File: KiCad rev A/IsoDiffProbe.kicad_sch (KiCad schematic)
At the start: 82 parts, among them J1 USB C 6-Pin, J2 SMA Conn, P1 Header 10X2, U1 AMC33xx, U2 OPA2376

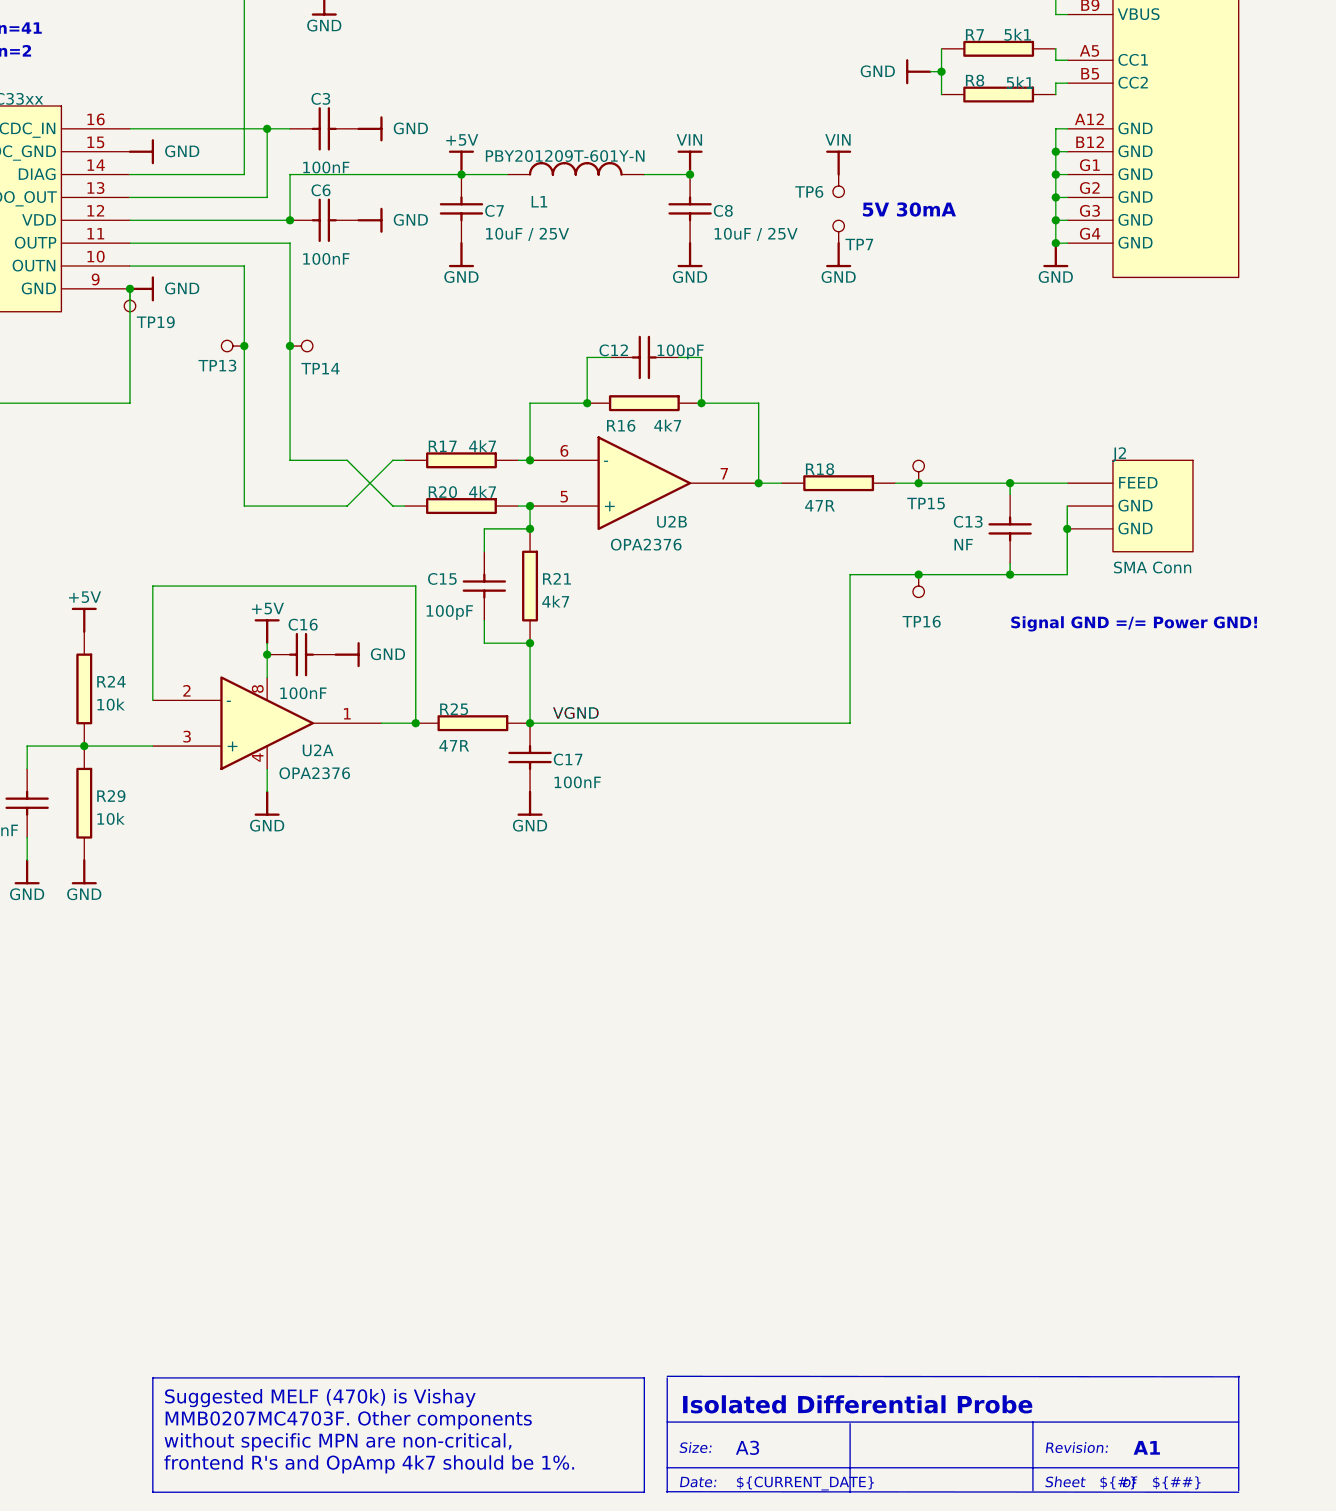
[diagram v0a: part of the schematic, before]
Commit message: Value changes to improve rev A1->A2 and updated rev B design.
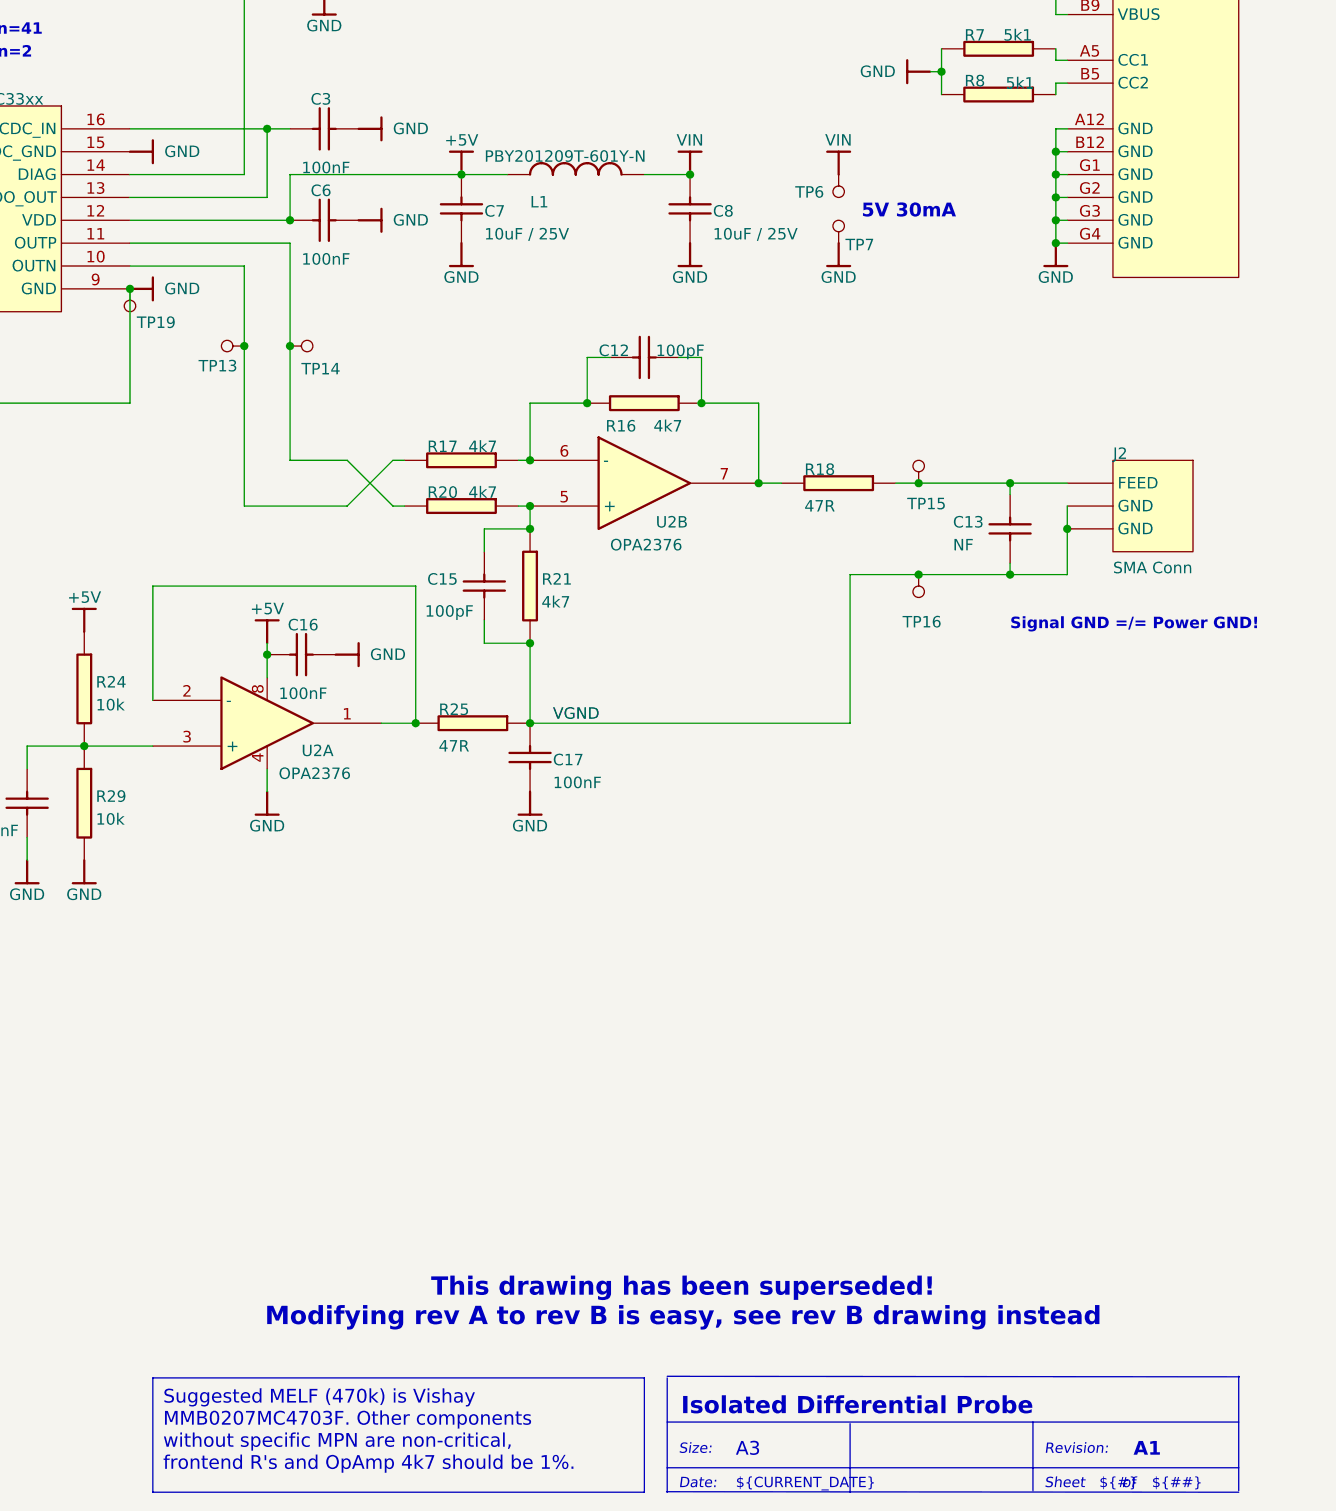
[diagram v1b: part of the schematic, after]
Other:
- note added: "This drawing has been superseded! Modifying rev A to rev B is easy, see rev B drawing instead"
